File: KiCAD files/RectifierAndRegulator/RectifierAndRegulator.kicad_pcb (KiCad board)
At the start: 2 copper layers, 73.7 x 27.9 mm, 12 parts, among them J1 Input, J2 Output, U1 L7805

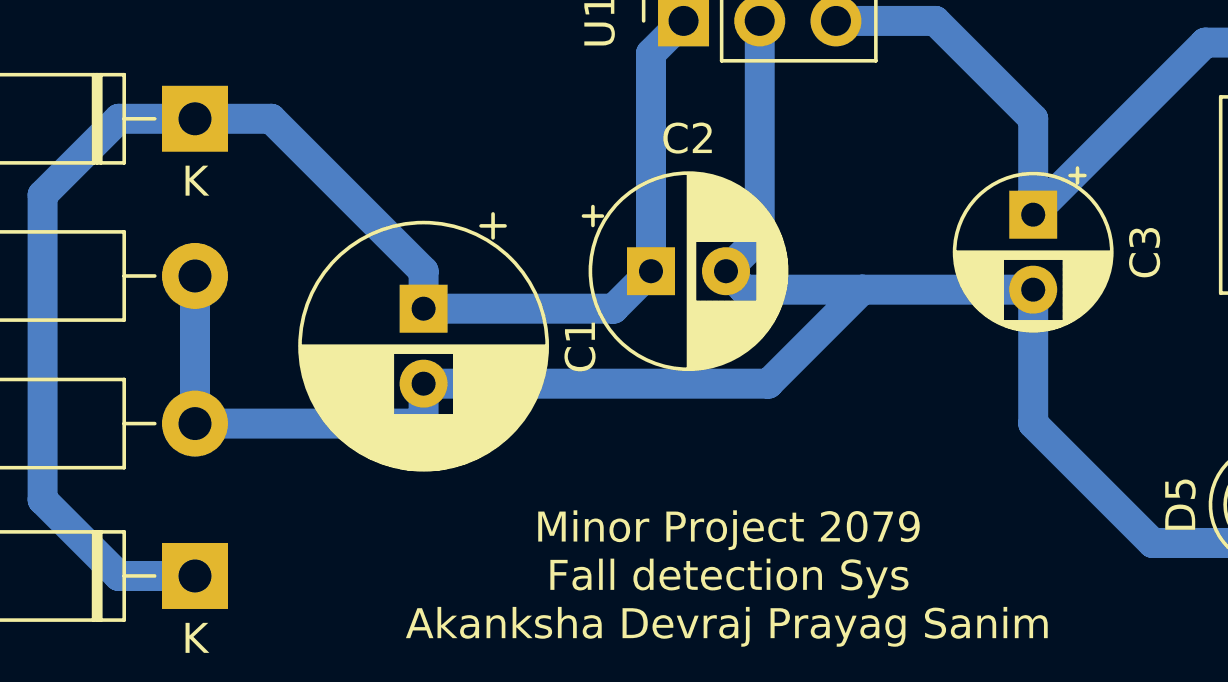
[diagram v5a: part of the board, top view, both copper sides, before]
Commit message: edited size of capacitor footprint
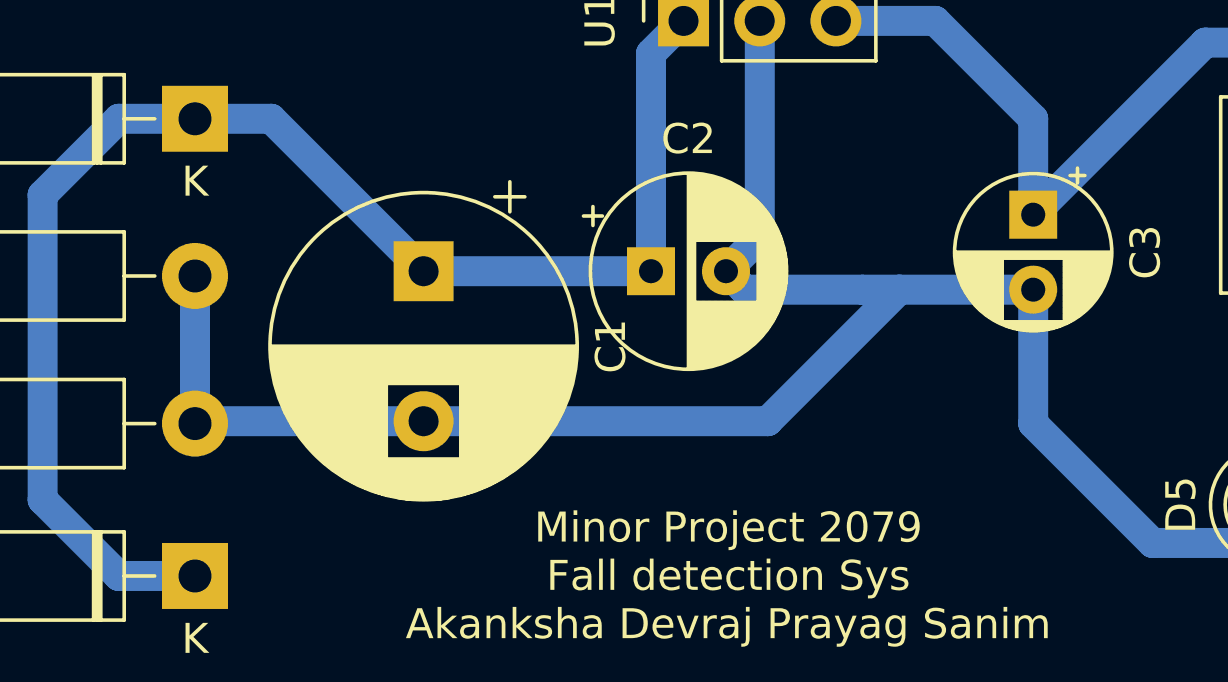
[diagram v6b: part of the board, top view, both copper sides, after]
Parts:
- C1: footprint Capacitor_THT:CP_Radial_D8.0mm_P2.50mm -> Capacitor_THT:CP_Radial_D10.0mm_P5.00mm
- moved C1 1.25 mm to (99.1, 121.9)
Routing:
- net Net-(C1-Pad1): track 50.3 -> 48.5 mm

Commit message: files merge
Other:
- board text added: "Minor Project 2079 Fall detection Sys Akanksha Devr Prayag Sanim"
- board text removed: "Minor Project 2079 Fall detection Sys Akanksha Devraj Prayag Sanim"
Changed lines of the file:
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@@
   )
   (gr_rect (start 68.58 109.22) (end 142.24 137.16) (layer "Edge.Cuts") (width 0.1) (fill none))
-  (gr_text "Minor Project 2079\nFall detection Sys\nAkanksha Devraj Prayag Sanim" (at 109.22 132.08) (layer "F.SilkS")
+  (gr_text "Minor Project 2079\nFall detection Sys\nAkanksha Devr Prayag Sanim" (at 109.22 132.08) (layer "F.SilkS")
     (effects (font (size 1 1) (thickness 0.15)))
   )

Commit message: rectifier pcb prints update
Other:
- board text added: "Minor Project 2079 Fall detection Sys Akanksha Dev Prayag Sanim"
- board text removed: "Minor Project 2079 Fall detection Sys Akanksha Devr Prayag Sanim"
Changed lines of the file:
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@@
       (effects (font (size 1 1) (thickness 0.15)))
     )
-    (fp_text value "Output" (at 2.54 2.37 90) (layer "F.Fab")
+    (fp_text value "Output" (at 2.54 2.37 90) (layer "F.SilkS")
       (effects (font (size 1 1) (thickness 0.15)))
     )
@@
       (effects (font (size 1 1) (thickness 0.15)))
     )
-    (fp_text value "Input" (at 2.54 2.37 90) (layer "F.Fab")
+    (fp_text value "Input" (at 2.54 2.37 90) (layer "F.SilkS")
       (effects (font (size 1 1) (thickness 0.15)))
     )
@@
       (effects (font (size 1 1) (thickness 0.15)))
     )
-    (fp_text value "L7805" (at 0 7.85 90) (layer "F.Fab")
+    (fp_text value "L7805" (at 0 7.85 90) (layer "F.SilkS")
       (effects (font (size 1 1) (thickness 0.15)))
     )
@@
   )
   (gr_rect (start 68.58 109.22) (end 142.24 137.16) (layer "Edge.Cuts") (width 0.1) (fill none))
-  (gr_text "Minor Project 2079\nFall detection Sys\nAkanksha Devr Prayag Sanim" (at 109.22 132.08) (layer "F.SilkS")
+  (gr_text "Minor Project 2079\nFall detection Sys\nAkanksha Dev Prayag Sanim" (at 109.22 132.08) (layer "F.SilkS")
     (effects (font (size 1 1) (thickness 0.15)))
   )
